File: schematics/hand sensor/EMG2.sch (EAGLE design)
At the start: 35 parts, among them IC1 INA118P, IC2 OP275P, IC3 OP275P, IC5 OP275P

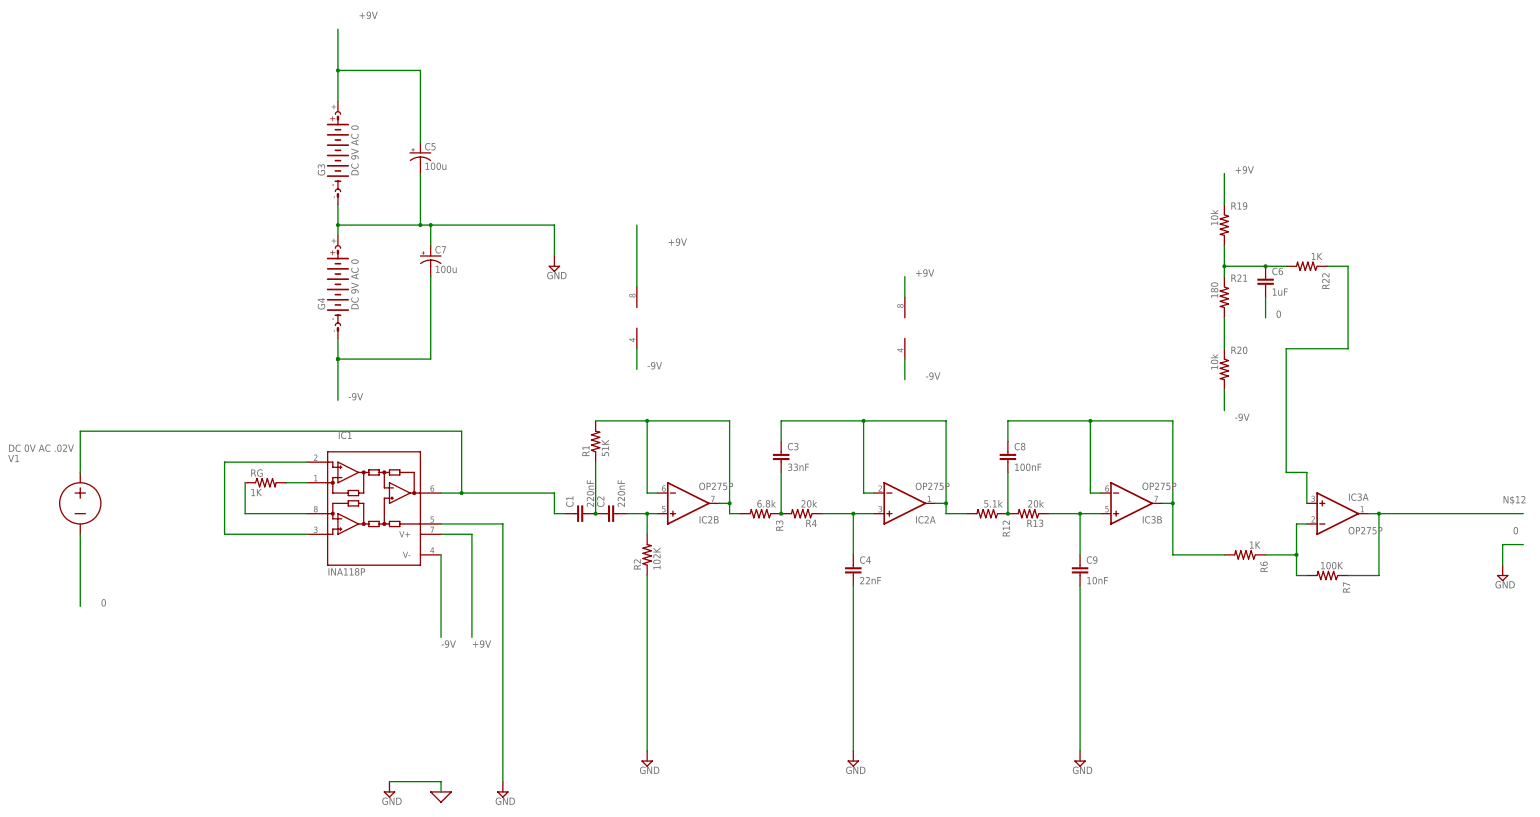
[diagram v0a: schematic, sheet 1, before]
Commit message: Implement socket transfering
Implement socket transfering between Python and Unity.
Arduino now has IR sensor implemented.
Record 10 signal from sensor (before fix).
Implement and train several models.
Implement data analytic module.
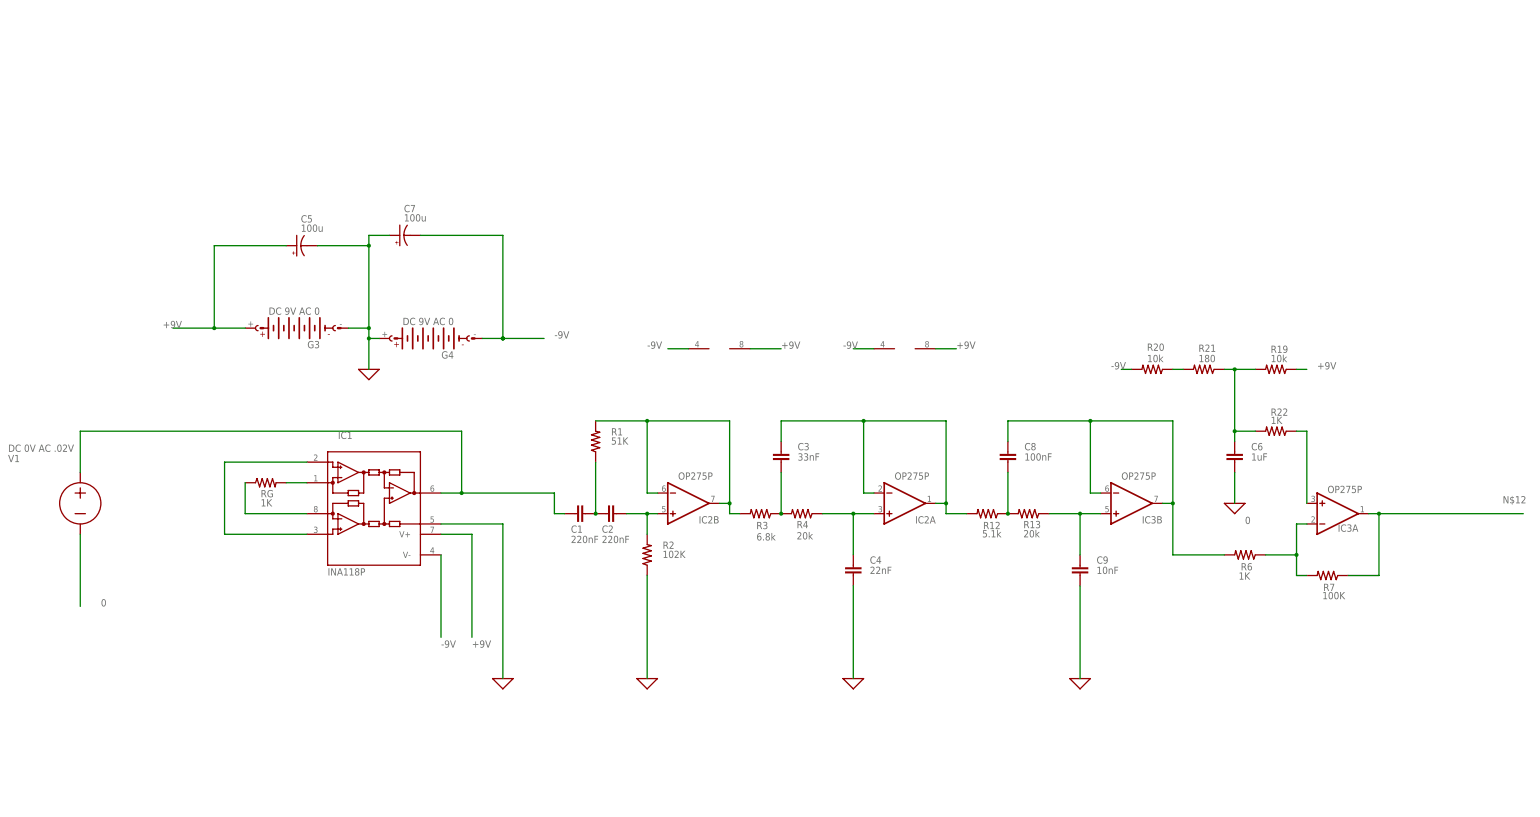
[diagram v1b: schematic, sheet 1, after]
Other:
- moved on the sheet: C5, C6, C7, G3, G4, R19, R20, R21, R22
